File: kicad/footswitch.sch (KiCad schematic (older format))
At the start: 20 parts

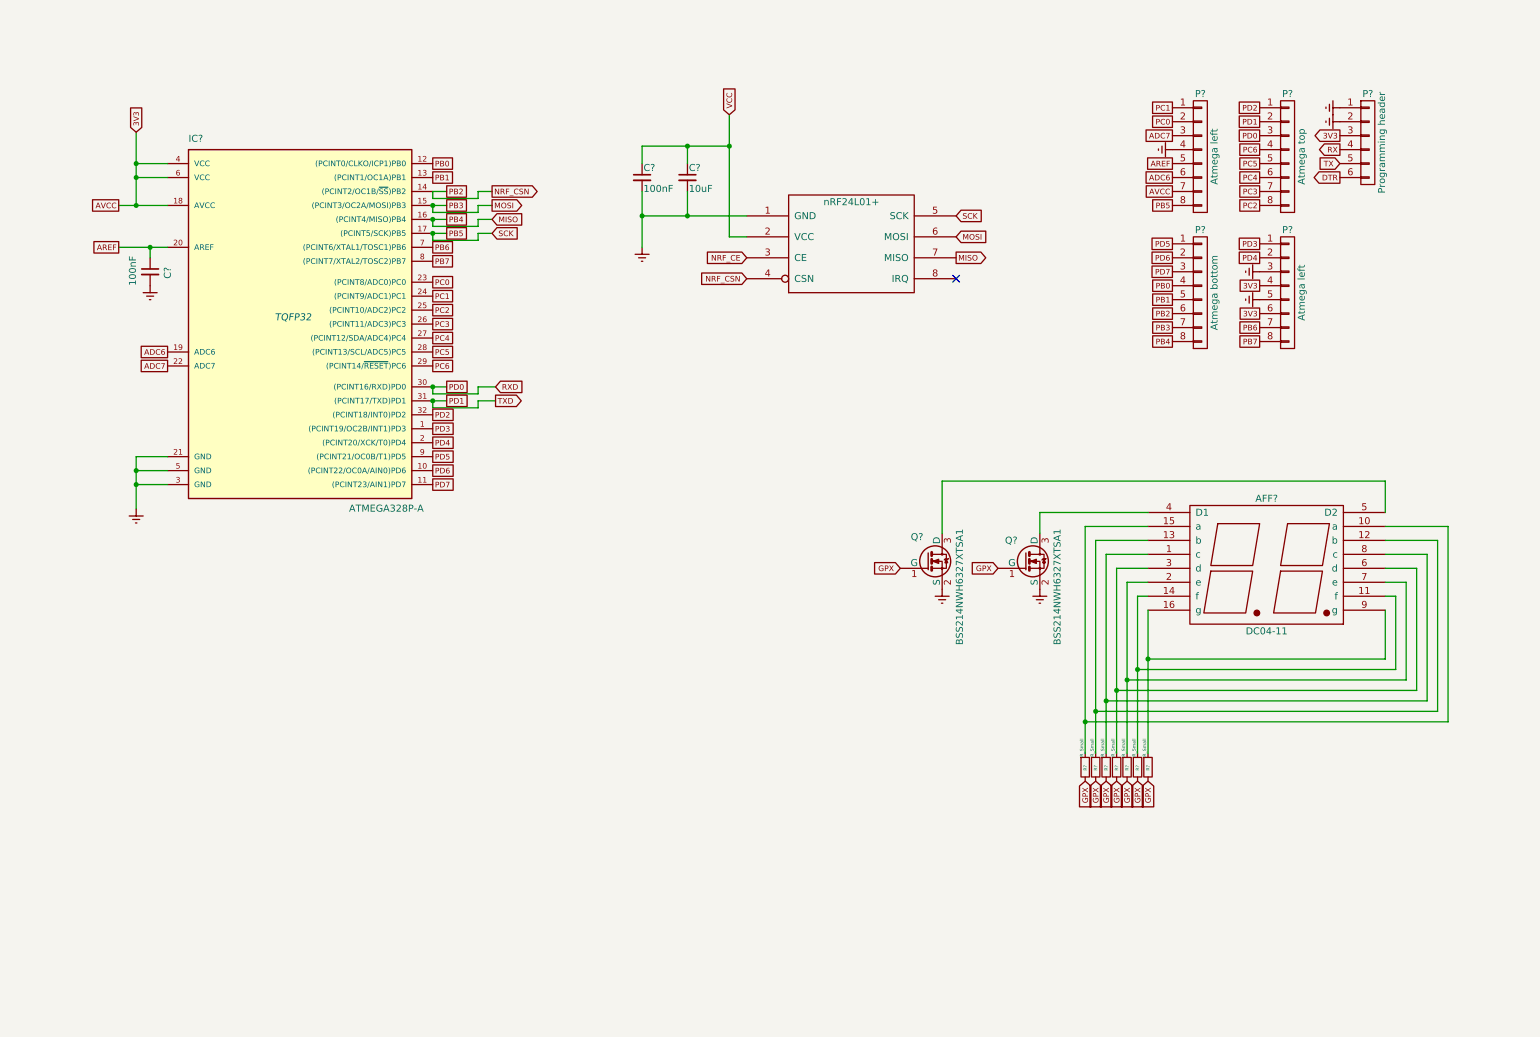
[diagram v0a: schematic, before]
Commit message: Add boost converter
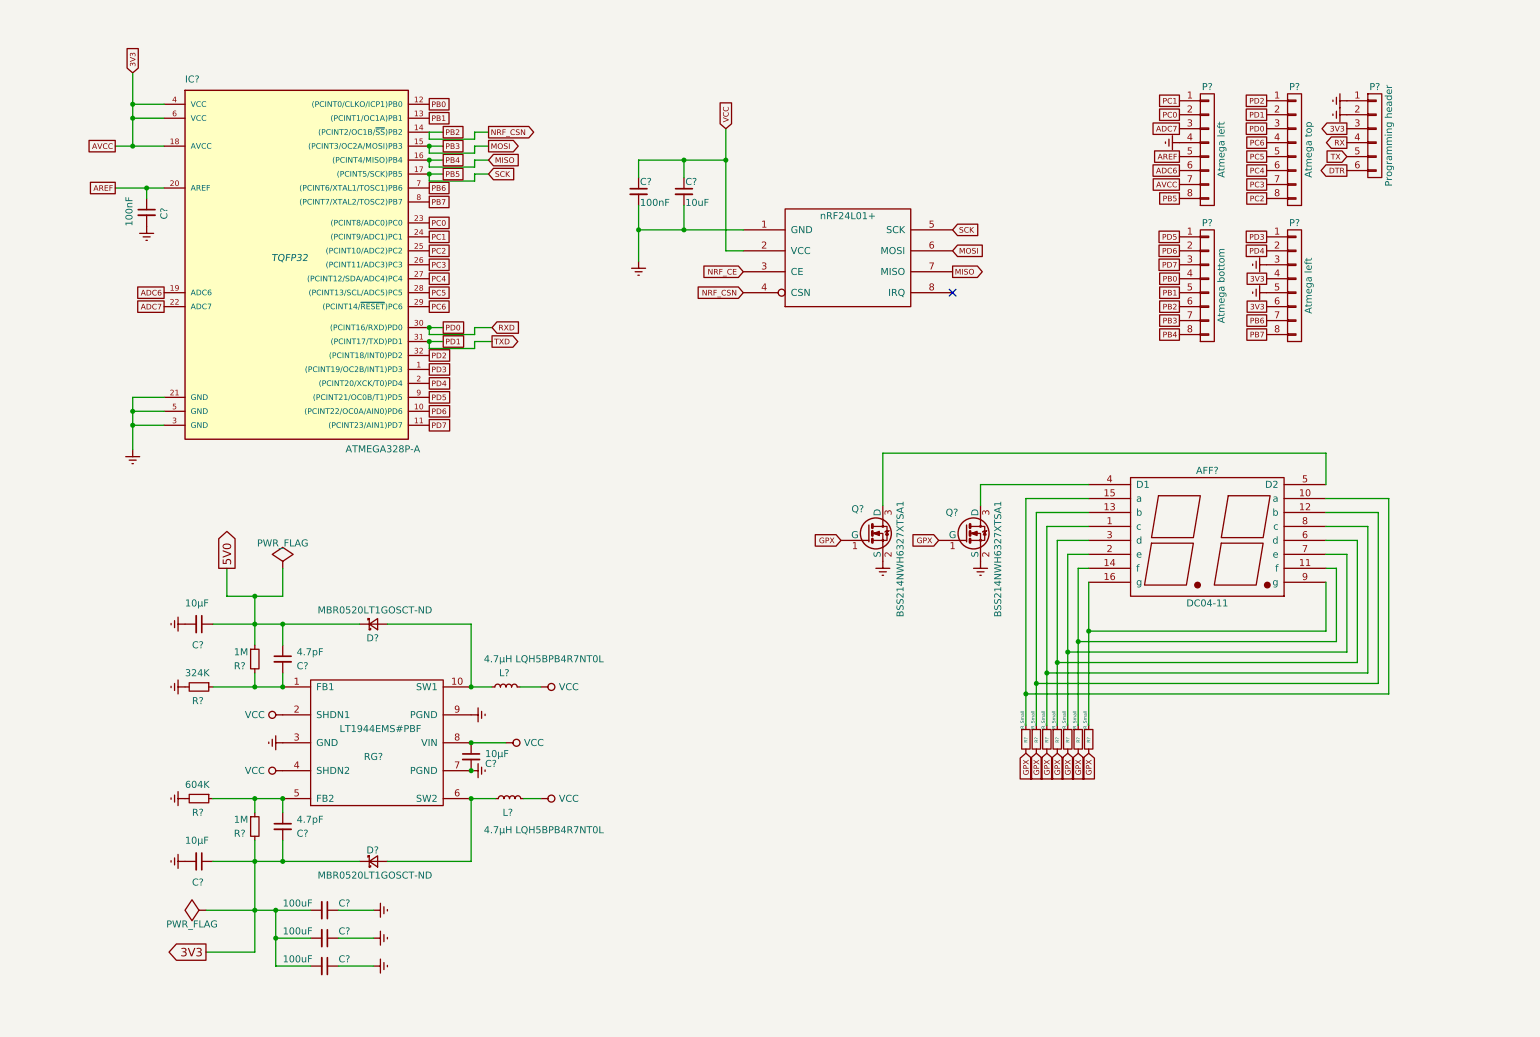
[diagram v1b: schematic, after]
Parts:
- added C? (x3): 10µF, Capacitors_SMD:C_0805_HandSoldering, symbol C_Small
- added C? (x2): 4.7pF, Capacitors_SMD:C_0805_HandSoldering, symbol C_Small
- added C? (x3): 100uF, Capacitors_SMD:C_1206_HandSoldering, symbol C_Small
- added D? (x2): MBR0520LT1GOSCT-ND, Diodes_SMD:SOD-123, symbol D_Schottky_Small
- added L? (x2): 4.7µH LQH5BPB4R7NT0L, symbol L_Small
- added R? (x2): 1M, Resistors_SMD:R_0805_HandSoldering, symbol R_Small
- added R?: 324K, Resistors_SMD:R_0805_HandSoldering, symbol R_Small
- added R?: 604K, Resistors_SMD:R_0805_HandSoldering, symbol R_Small
- added RG?: LT1944EMS#PBF, Housings_SSOP:MSOP-10_3x3mm_Pitch0.5mm, symbol LT1944
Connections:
- net 3V3: now also C?.1, C?.2, C?.2, C?.2, C?.2, D?.1 (K), R?.2
- net Earth: now also C?.1, C?.1, C?.1, C?.2, C?.2, C?.2, R?.2, R?.2, RG?.3 (GND), RG?.7 (PGND), RG?.9 (PGND)
- net VCC: now also C?.1, L?.2, L?.2, RG?.2 (SHDN1), RG?.4 (SHDN2), RG?.8 (VIN)
- new net: D?.2 (A), L?.1, RG?.6 (SW2)
- new net: D?.2 (A), L?.1, RG?.10 (SW1)
- new net: C?.2, R?.1, R?.2, RG?.1 (FB1)
- new net: C?.1, R?.1, R?.1, RG?.5 (FB2)
- new net 5V0: C?.1, C?.1, D?.1 (K), R?.1
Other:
- moved on the sheet: AFF?, C?, IC?, P?, Q?, R?

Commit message: Continue schematic
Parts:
- removed C?: 4.7pF, Capacitors_SMD:C_0805_HandSoldering, symbol C_Small
- removed C?: 10µF, Capacitors_SMD:C_0805_HandSoldering, symbol C_Small
- removed D?: MBR0520LT1GOSCT-ND, Diodes_SMD:SOD-123, symbol D_Schottky_Small
- removed L?: 4.7µH LQH5BPB4R7NT0L, symbol L_Small
- removed R?: 1M, Resistors_SMD:R_0805_HandSoldering, symbol R_Small
- removed R?: 324K, Resistors_SMD:R_0805_HandSoldering, symbol R_Small
- added BT?: Battery_Cell, symbol Battery_Cell
- added C? (x2): C_Small, symbol C_Small
- added C? (x2): 100nF, symbol C_Small
- added C?: 10uF, symbol C_Small
- added R? (x2): 100, symbol R_Small
- added R?: 10K, symbol R_Small
- added R? (x6): 10K, Resistors_SMD:R_0805_HandSoldering, symbol R_Small
- added RV?: POT, symbol POT
- added SW? (x6): SW_SPST, symbol SW_SPST
- added SW?: SW_RST, symbol SW_SPST
- added U?: CD4072BM96, symbol CD4072BM96
- added Y?: Crystal_Small, symbol Crystal_Small
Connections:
- net 3V3: now also C?.1, C?.1, R?.1, R?.1, R?.1, R?.1, R?.1, R?.1, R?.1, U?.14 (VDD)
- net ADC6: no longer IC?.19 (ADC6)
- net ADC7: no longer IC?.22 (ADC7)
- net DTR: now also C?.2
- net Earth: now also RG?.2 (SHDN1), C?.2, C?.2, C?.2, C?.2, SW?.1 (A), SW?.1 (A), SW?.1 (A), SW?.1 (A), SW?.1 (A), SW?.1 (A), SW?.2 (B), U?.7 (VSS)
- net MISO: no longer P?.8 (P8)
- net MOSI: no longer P?.7 (P7)
- net NRF_CSN: no longer IC?.14 ((PCINT2/OC1B/~SS~)PB2), P?.6 (P6)
- net PB0: no longer IC?.12 ((PCINT0/CLKO/ICP1)PB0)
- net PB1: no longer IC?.13 ((PCINT1/OC1A)PB1)
- net PB5: no longer IC?.17 ((PCINT5/SCK)PB5), U?.5 (SCK)
- net PB6: now also C?.1, Y?.1; no longer IC?.7 ((PCINT6/XTAL1/TOSC1)PB6)
- net PB7: now also C?.1, Y?.2; no longer IC?.8 ((PCINT7/XTAL2/TOSC2)PB7)
- net PC0: no longer IC?.23 ((PCINT8/ADC0)PC0)
- net PC1: no longer IC?.24 ((PCINT9/ADC1)PC1)
- net PC2: no longer IC?.25 ((PCINT10/ADC2)PC2)
- net PC3: no longer IC?.26 ((PCINT11/ADC3)PC3)
- net PC4: no longer IC?.27 ((PCINT12/SDA/ADC4)PC4)
- net PC5: no longer IC?.28 ((PCINT13/SCL/ADC5)PC5)
- net PC6: no longer IC?.29 ((PCINT14/~RESET~)PC6)
- net PD0: no longer IC?.30 ((PCINT16/RXD)PD0)
- net PD1: no longer IC?.31 ((PCINT17/TXD)PD1)
- net PD2: no longer IC?.32 ((PCINT18/INT0)PD2)
- net PD3: no longer IC?.1 ((PCINT19/OC2B/INT1)PD3)
- net PD4: no longer IC?.2 ((PCINT20/XCK/T0)PD4)
- net PD5: no longer IC?.9 ((PCINT21/OC0B/T1)PD5)
- net PD6: no longer IC?.10 ((PCINT22/OC0A/AIN0)PD6)
- net PD7: no longer IC?.11 ((PCINT23/AIN1)PD7)
- net VCC: no longer RG?.2 (SHDN1)
- removed net GPX: Q?.1 (G), Q?.1 (G), R?.2, R?.2, R?.2, R?.2, R?.2, R?.2, R?.2
- new net: C?.1, IC?.29 ((PCINT14/~RESET~)PC6), R?.2, SW?.1 (A)
- new net: Q?.1 (G), R?.2 (x2)
- new net: U?.1 (A+B+C+D), U?.11 (G)
- new net A0: IC?.23 ((PCINT8/ADC0)PC0)
- new net A1: IC?.24 ((PCINT9/ADC1)PC1), R?.2
- new net A2: IC?.25 ((PCINT10/ADC2)PC2), R?.2
- new net A3: IC?.26 ((PCINT11/ADC3)PC3), R?.2
- new net A6: IC?.19 (ADC6), R?.2
- new net A7: IC?.22 (ADC7), R?.2
- new net D10: IC?.14 ((PCINT2/OC1B/~SS~)PB2), R?.1
- new net D2: IC?.32 ((PCINT18/INT0)PD2), U?.13 (E+F+G+H)
- new net D3: IC?.1 ((PCINT19/OC2B/INT1)PD3), R?.2, SW?.2 (B), U?.2 (A)
- new net D4: IC?.2 ((PCINT20/XCK/T0)PD4), R?.2, SW?.2 (B), U?.3 (B)
- new net D5: IC?.9 ((PCINT21/OC0B/T1)PD5), R?.2, SW?.2 (B), U?.4 (C)
- new net D6: IC?.10 ((PCINT22/OC0A/AIN0)PD6), R?.2, SW?.2 (B), U?.5 (D)
- new net D7: IC?.11 ((PCINT23/AIN1)PD7), R?.2, SW?.2 (B), U?.9 (E)
- new net D8: IC?.12 ((PCINT0/CLKO/ICP1)PB0), R?.2, SW?.2 (B), U?.10 (F)
- new net D9: IC?.13 ((PCINT1/OC1A)PB1), R?.1
- new net PB2: P?.6 (P6)
- new net PB3: P?.7 (P7)
- new net PB4: P?.8 (P8)
- new net RXI: IC?.30 ((PCINT16/RXD)PD0)
- new net SCK: IC?.17 ((PCINT5/SCK)PB5), U?.5 (SCK)
- new net SCL: IC?.28 ((PCINT13/SCL/ADC5)PC5), R?.2
- new net SDA: IC?.27 ((PCINT12/SDA/ADC4)PC4), R?.2
- new net TXO: IC?.31 ((PCINT17/TXD)PD1)
- new net XTAL1: IC?.7 ((PCINT6/XTAL1/TOSC1)PB6)
- new net XTAL2: IC?.8 ((PCINT7/XTAL2/TOSC2)PB7)
- no-connect marks 1 -> 6
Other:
- moved on the sheet: AFF?, C?, D?, IC?, L?, P?, Q?, R?, RG?

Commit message: Continue schematic
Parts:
- removed R? (x3): 10K, Resistors_SMD:R_0805_HandSoldering, symbol R_Small
- removed SW? (x3): SW_SPST, symbol SW_SPST
- added P?: Pot hdr, symbol CONN_01X03
- added P?: App select, symbol CONN_01X02
- added R? (x6): 10K, Resistors_SMD:R_0805_HandSoldering, symbol R_Small
- added R?: 10K, symbol R_Small
- added SW? (x5): SW_SPST, symbol SW_SPST
- P?: symbol CONN_01X08 -> CONN_01X06
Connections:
- net ADC6 is gone; now on net A6: P?.6 (P6)
- net ADC7 is gone; now on net A7: P?.3 (P3)
- net NRF_CE is gone; now on net D6: U?.3 (CE)
- net NRF_CSN is gone; now on net D7: U?.4 (CSN)
- net PB0 is gone; now on net D8: P?.4 (P4)
- net PB1 is gone; now on net D9: P?.5 (P5)
- net PB2 is gone; now on net D10: P?.6 (P6)
- net PB3 is gone; now on net MOSI: P?.7 (P7)
- net PB4 is gone; now on net MISO: P?.8 (P8)
- net PB5 is gone; now on net SCK: P?.8 (P8)
- net PC0 is gone; now on net A0: P?.2 (P2)
- net PC1 is gone; now on net A1: P?.1 (P1)
- net PC2 is gone; now on net A2: P?.8 (P8)
- net PC3 is gone; now on net A3: P?.7 (P7)
- net PC4 is gone; now on net SDA: P?.6 (P6)
- net PC5 is gone; now on net SCL: P?.5 (P5)
- net PC6 is gone; now on net RESET: P?.4 (P4)
- net PD0 is gone; now on net RXI: P?.3 (P3)
- net PD1 is gone; now on net TXO: P?.2 (P2)
- net PD2 is gone; now on net D2: P?.1 (P1)
- net PD3 is gone; now on net D3: P?.1 (P1)
- net PD4 is gone; now on net D4: P?.2 (P2)
- net PD5 is gone; now on net D5: P?.1 (P1)
- net PD6 is gone; now on net D6: P?.2 (P2)
- net PD7 is gone; now on net D7: P?.3 (P3)
- net 3V3: now also P?.1 (P1), R?.1, R?.1, R?.1, R?.1, R?.1
- net A1: now also R?.2, SW?.2 (B), U?.4 (C)
- net A2: now also U?.9 (E), R?.2, SW?.2 (B)
- net A3: now also U?.10 (F), R?.2, SW?.2 (B)
- net A7: now also RV?.2; no longer R?.2
- net D2: now also U?.1 (A+B+C+D); no longer U?.13 (E+F+G+H)
- net D3: now also R?.2, SW?.2 (B); no longer R?.2, SW?.2 (B), U?.2 (A)
- net D4: now also R?.2, SW?.2 (B), U?.2 (A); no longer R?.2, SW?.2 (B), U?.3 (B)
- net D5: now also R?.2, SW?.2 (B), U?.3 (B); no longer R?.2, SW?.2 (B), U?.4 (C)
- net D6: now also R?.1; no longer U?.5 (D)
- net D7: now also R?.1; no longer U?.9 (E)
- net D8: now also R?.2; no longer U?.10 (F)
- net Earth: now also BT?.2 (-), RV?.1, R?.2, SW?.1 (A), SW?.1 (A), SW?.1 (A), SW?.1 (A), SW?.1 (A)
- net PB6: no longer P?.7 (P7)
- net PB7: no longer P?.8 (P8)
- net SCL: now also U?.12 (H), R?.2, SW?.2 (B)
- net SDA: now also U?.11 (G), R?.2, SW?.2 (B)
- net TXO: now also P?.3 (P3)
- net VCC: now also BT?.1 (+), R?.2
- net RESET: now reaches C?.1, IC?.29 ((PCINT14/~RESET~)PC6), R?.2, SW?.1 (A)
- net at RV?.3: now also P?.2 (P2)
- new net: P?.2 (P2), U?.13 (E+F+G+H)
- new net: P?.1 (P1), U?.5 (D)
- no-connect marks 6 -> 5
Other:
- moved on the sheet: BT?, C?, D?, IC?, L?, P?, R?, RG?, RV?, SW?, U?, Y?
